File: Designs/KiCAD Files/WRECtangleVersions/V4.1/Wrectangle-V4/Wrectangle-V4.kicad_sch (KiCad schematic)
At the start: 66 parts, among them J10 xBee-Antenna1, J2 USB_C_Receptacle_USB2.0_16P, J3 AnalogIn-Terminal3, J4 AnalogIn-Terminal2, J5 AnalogIn-Terminal1, J6 AnalogIn-Terminal0, J7 GPS-Antenna, J8 Micro_SD_Card, U1 STM32F405RGTx, U10 FT232RL, U11 BME280, U2 BNO085_C5189642, U3 MAX-M10S-00B, U4 H3LIS331DLTR, U9 XBP9X-DMUS-001

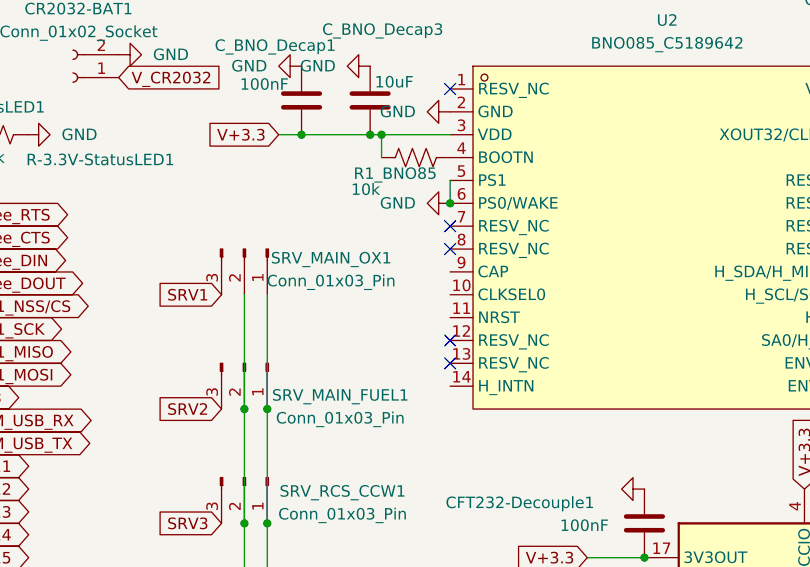
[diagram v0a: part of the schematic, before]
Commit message: Added a capacitor to CAP on BNO85
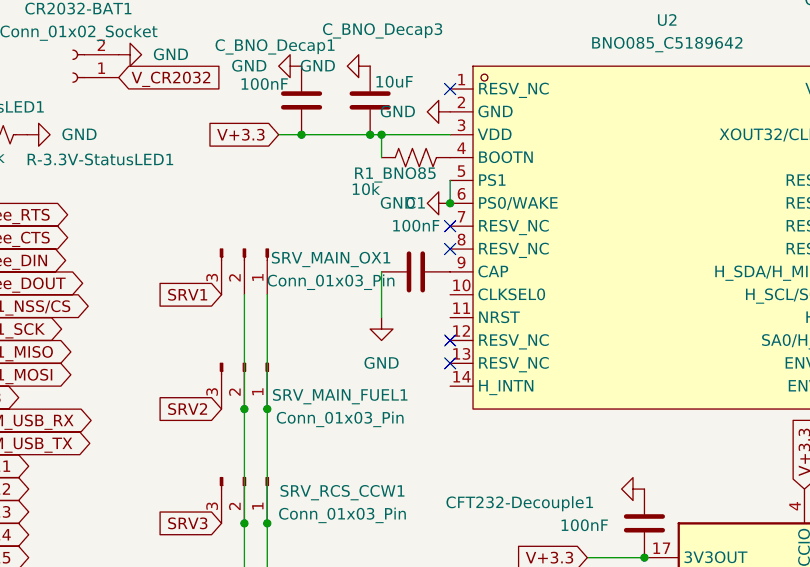
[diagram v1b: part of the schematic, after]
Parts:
- added C1: 100nF, symbol Device:C
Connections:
- net GND: now also C1.1
- net at U2.9 (CAP): now also C1.2
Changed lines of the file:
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@@
 	(wire
 		(pts
+			(xy 127 48.26) (xy 127 43.18)
+		)
+		(stroke
+			(width 0)
+			(type default)
+		)
+	)
+	(wire
+		(pts
 			(xy 184.15 66.04) (xy 179.07 66.04)
 		)
@@
 	)
 	(symbol
+		(lib_id "Device:C")
+		(at 130.81 43.18 90)
+		(unit 1)
+		(exclude_from_sim no)
+		(in_bom yes)
+		(on_board yes)
+		(dnp no)
+		(fields_autoplaced yes)
+		(property "Reference" "C1"
+			(at 130.81 35.56 90)
+			(effects
+				(font
+					(size 1.27 1.27)
+				)
+			)
+		)
+		(property "Value" "100nF"
+			(at 130.81 38.1 90)
+			(effects
+				(font
+					(size 1.27 1.27)
+				)
+			)
+		)
+		(property "Footprint" ""
+			(at 134.62 42.2148 0)
+			(effects
+				(font
+					(size 1.27 1.27)
+				)
+				(hide yes)
+			)
+		)
+		(property "Datasheet" "~"
+			(at 130.81 43.18 0)
+			(effects
+				(font
+					(size 1.27 1.27)
+				)
+				(hide yes)
+			)
+		)
+		(property "Description" "Unpolarized capacitor"
+			(at 130.81 43.18 0)
+			(effects
+				(font
+					(size 1.27 1.27)
+				)
+				(hide yes)
+			)
+		)
+		(pin "1"
+		)
+		(pin "2"
+		)
+		(instances
+			(project ""
+				(path "/999a87cf-6a03-4be4-a445-b5341a1dddf0"
+					(reference "C1")
+					(unit 1)
+				)
+			)
+		)
+	)
+	(symbol
 		(lib_id "Device:LED")
 		(at 208.28 100.33 0)
@@
 					(unit 1)
 				)
+			)
+		)
+	)
+	(symbol
+		(lib_id "power:GND")
+		(at 127 48.26 0)
+		(unit 1)
+		(exclude_from_sim no)
+		(in_bom yes)
+		(on_board yes)
+		(dnp no)
+		(fields_autoplaced yes)
+		(property "Reference" "#PWR080"
+			(at 127 54.61 0)
+			(effects
+				(font
+					(size 1.27 1.27)
+				)
+				(hide yes)
+			)
+		)
+		(property "Value" "GND"
+			(at 127 53.34 0)
+			(effects
+				(font
+					(size 1.27 1.27)
+				)
+			)
+		)
+		(property "Footprint" ""
+			(at 127 48.26 0)
+			(effects
+				(font
+					(size 1.27 1.27)
+				)
+				(hide yes)
+			)
+		)
+		(property "Datasheet" ""
+			(at 127 48.26 0)
+			(effects
+				(font
+					(size 1.27 1.27)
+				)
+				(hide yes)
+			)
+		)
+		(property "Description" "Power symbol creates a global label with name \"GND\" , ground"
+			(at 127 48.26 0)
+			(effects
+				(font
+					(size 1.27 1.27)
+				)
+				(hide yes)
+			)
+		)
+		(pin "1"
+		)
+		(instances
+			(project "Wrectangle-V4"
+				(path "/999a87cf-6a03-4be4-a445-b5341a1dddf0"
+					(reference "#PWR080")
+					(unit 1)
+				)

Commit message: h
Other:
- note added: "luke edit test"
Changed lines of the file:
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@@
+		)
+	)
+	(text "luke edit test"
+		(exclude_from_sim no)
+		(at 24.638 130.048 0)
+		(effects
+			(font
+				(size 1.27 1.27)
+			)
 		)
 	)
